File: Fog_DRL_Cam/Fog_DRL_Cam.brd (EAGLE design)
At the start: 80 x 60 mm, 51 parts, among them IC1 78L05Z, IC2 TINY13-20SSU, IC3 TINY13-20SSU, K1 CQ1-12V, K2 CQ1-12V, Q1 SI2302, X1 RCAX2, X10 PROG-ISP6POGOPIN, X11 PROG-ISP6POGOPIN, X2 PS/2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

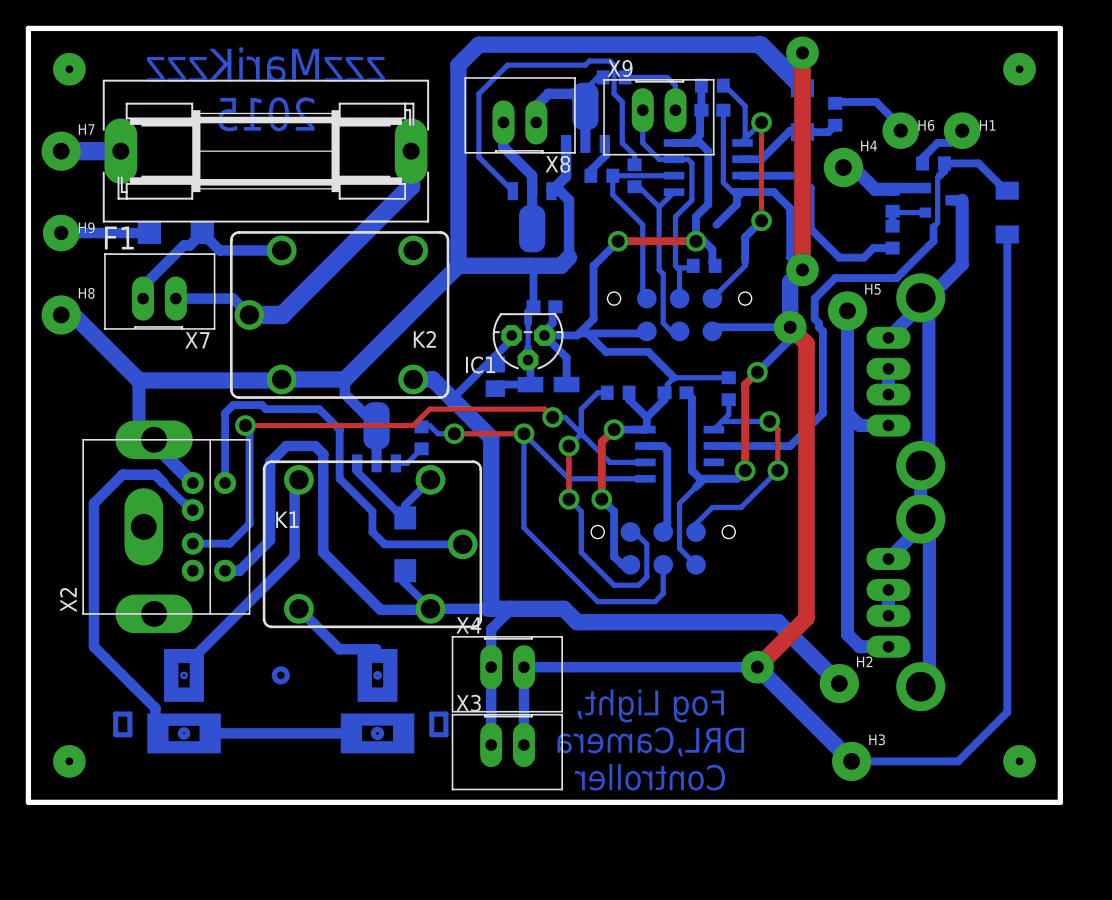
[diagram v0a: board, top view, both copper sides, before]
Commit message: Добавлены ДХО работающие на ШИМ
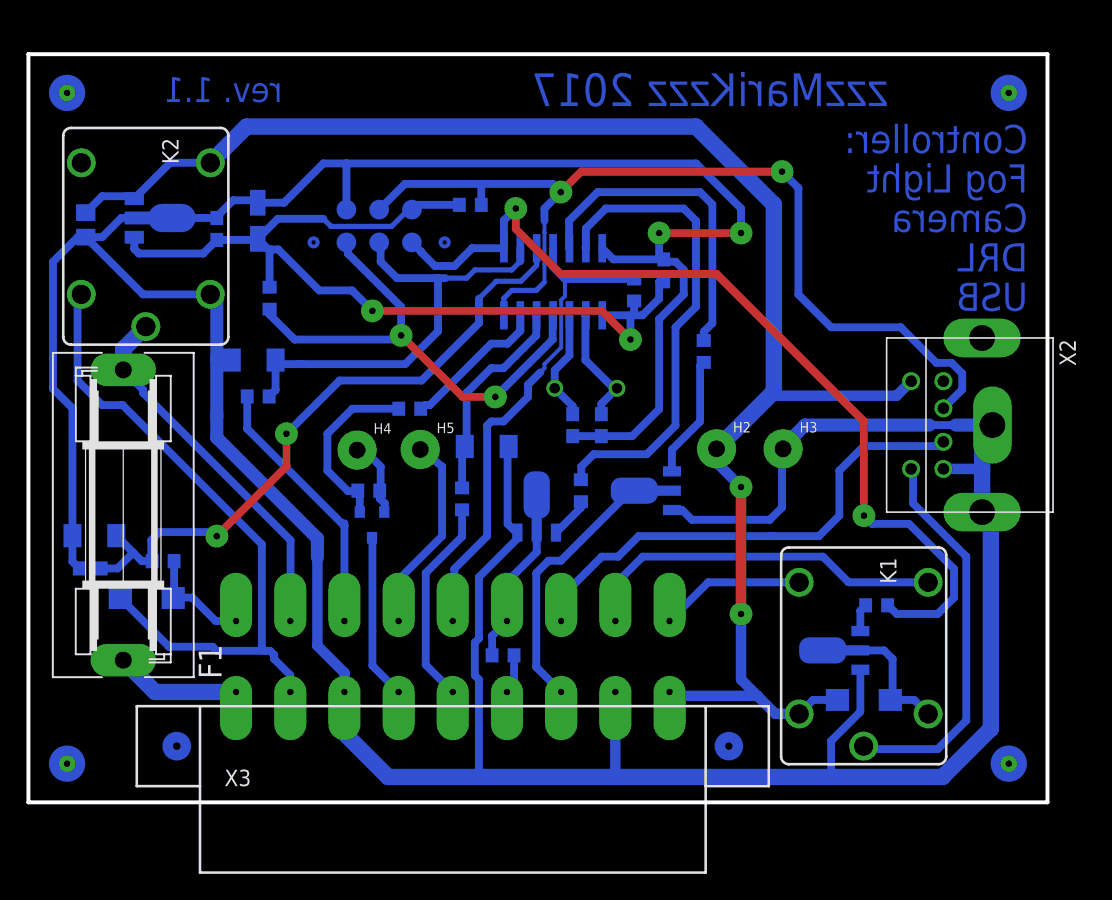
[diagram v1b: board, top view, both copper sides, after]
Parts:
- removed C3: (no value), rcl:C0603
- removed H1: Reverse, holes:2,8
- removed H6: Bliz, holes:2,8
- removed H7: +12V, holes:3,0
- removed H8: GND, holes:3,0
- removed H9: Mar, holes:2,8
- removed IC2, IC3: TINY13-20SSU, atmel:8S1
- removed X10, X11: PROG-ISP6POGOPIN, usb:PROG_POGOPIN
- removed X4, X7, X8, X9: JST2, usb:JST*2
- removed X5, X6: USB-FEMALE, usb:USB-FEMALE
- added C6, C7: 22pF, rcl:C0603
- added D5: (no value), diode:SOD80C
- added Q2: 16MHz, crystal:HC49/S
- added R13: 10k, rcl:R0603
- added U1: ATTINY24A-SU, usb:SO14
- C4: value (none) -> 100n
- IC1: value 78L05Z -> 78L05F; device linear:TO92 -> linear:SOT89
- Q1: value SI2302 -> IRLML2502
- R6: value 10k -> 2k2
- X1: value RCAX2 -> PROG-ISP6POGOPIN; device usb:RCAX2 -> usb:PROG_POGOPIN
- X3: value JST2 -> MOLEX18; device usb:JST*2 -> usb:MOLEX18
- moved R6 56.3 mm to (10.4, 18.7), turned to 180 degrees
- moved X2 53.8 mm to (66.5, 36.0), turned to 270 degrees
- moved R4 49.8 mm to (17.8, 31.5), turned to 0 degrees
- moved Q1 49.2 mm to (26.6, 22.5), turned to 180 degrees
- moved D3 46.7 mm to (17.5, 34.3), turned to 0 degrees
- moved R3 46.4 mm to (26.4, 24.2), turned to 0 degrees
- moved R12 45.6 mm to (36.8, 11.4)
- moved R5 44.9 mm to (33.6, 23.5), turned to 270 degrees
- moved D4 44.2 mm to (35.5, 27.6), turned to 180 degrees
- moved H4 43.6 mm to (25.5, 27.3)
- moved R2 39.7 mm to (29.6, 30.5), turned to 0 degrees
- moved VT1 39.2 mm to (62.5, 11.8), turned to 270 degrees
- moved K1 39.0 mm to (64.8, 11.4), turned to 270 degrees
- moved R10 37.6 mm to (65.8, 15.3), turned to 0 degrees
- moved D1 37.6 mm to (64.8, 7.94), turned to 180 degrees
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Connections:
- removed net N$10: X6.D+, X6.D-
- removed net N$23: IC2.1, R6.1, X11.5
- removed net N$24: IC2.5, R8.1, X11.4
- removed net N$29: IC3.5, R10.1, X10.4
- removed net N$30: IC3.6, R11.2, X10.1, X2.1
- removed net N$9: X5.D+, X5.D-
- new net CAM_RELAY: R10.1, U1.8, X1.1
- new net MAR: D5.C, R13.1, R6.1, U1.10
- new net N$38: R9.2, U1.4, X1.5
- new net N$39: C7.1, Q2.2, U1.3
- new net REVERS_KEY: R11.2, U1.7, X1.4, X2.1
- net +12V: now also X3.P$17; no longer X3.1, X4.1
- net +5V: now also U1.1, X1.2; no longer C3.1, IC2.8, IC3.8, R6.2, X10.2, X11.2
- net BLIZHNIY: now also U1.9, X1.3; no longer IC2.2
- net GND: now also C6.2, C7.2, D5.A, IC1.2@1, R13.2, U1.14, VT1.E, X1.6, X2.GND2, X3.P$15, X3.P$5; no longer C3.2, H8.P$1, IC2.4, IC3.4, VT1.C, VT1.C@1, X10.6, X11.6, X3.2, X4.2
- net N$1: now also X3.P$16; no longer X1.AV1
- net N$11: now also X3.P$4; no longer X7.1
- net N$12: now also X3.P$3; no longer X7.2
- net N$13: now also R6.2, X3.P$2; no longer H9.P$1
- net N$14: now also U1.6; no longer IC2.3
- net N$15: now also X3.P$13; no longer X8.2
- net N$16: now also X3.P$12; no longer X8.1
- net N$17: now also R8.1, U1.12; no longer IC2.6, R7.1, X11.1
- net N$18: now also R7.1, U1.13; no longer IC3.7, X10.3
- net N$19: now also U1.11, X3.P$10; no longer IC2.7, X11.3, X9.1
- net N$2: now also X3.P$11; no longer X9.2
- net N$21: now also X3.P$9; no longer H1.P$1
- net N$22: now also X3.P$6; no longer H6.P$1
- net N$27: now also C6.1, Q2.1, U1.2; no longer IC3.1, R9.2, X10.5
- net N$3: now also X3.P$14; no longer X1.GND1, X1.GND2
- net N$31: now also X3.P$18; no longer X1.AV2
- net N$5: now also VT1.C, VT1.C@1; no longer VT1.E
- net N$6: now also X3.P$1; no longer H7.P$1
- net N$7: now also X3.P$8; no longer X5.VCC, X6.VCC
- net N$8: now also X3.P$7; no longer X5.GND, X5.GND@1, X5.GND@2, X6.GND, X6.GND@1, X6.GND@2
- net REVERSE: now also U1.5; no longer IC3.2
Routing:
- net REVERS_KEY: track 0.00 -> 75.8 mm, vias 0 -> 2
- net N$30: track 71.1 -> 0.00 mm, vias 4 -> 0
- net CAM_RELAY: track 0.00 -> 70.9 mm, vias 0 -> 2
- net MAR: track 0.00 -> 51.1 mm, vias 0 -> 2
- net N$29: track 42.1 -> 0.00 mm, vias 2 -> 0
- net N$38: track 0.00 -> 38.2 mm, vias 0 -> 2
- net N$12: track 14.0 -> 51.8 mm
- net N$8: track 49.6 -> 12.8 mm
- net N$18: track 8.31 -> 37.3 mm
- net BLIZHNIY: track 8.37 -> 35.4 mm
- net REVERSE: track 41.8 -> 16.8 mm
- net N$23: track 23.0 -> 0.00 mm, vias 2 -> 1
- net N$19: track 19.4 -> 38.8 mm
- net N$26: track 28.7 -> 9.47 mm
- net N$7: track 32.2 -> 15.6 mm
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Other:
- board size 80 x 60 mm -> 79 x 58 mm
- board text added: "Controller: Fog Light Camera DRL USB"
- board text added: "rev. 1.1"
- board text added: "zzzMariKzzz 2017"
- board text removed: "Fog Light, DRL,Camera Controller"
- board text removed: "zzzMariKzzz 2015"
